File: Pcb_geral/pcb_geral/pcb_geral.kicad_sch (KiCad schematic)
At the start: 29 parts, among them U1 LM2594M-3.3, U2 LM2596S-5, U3 STM32F103C6Tx, U4 TJA1051T, Y2 8Mhz

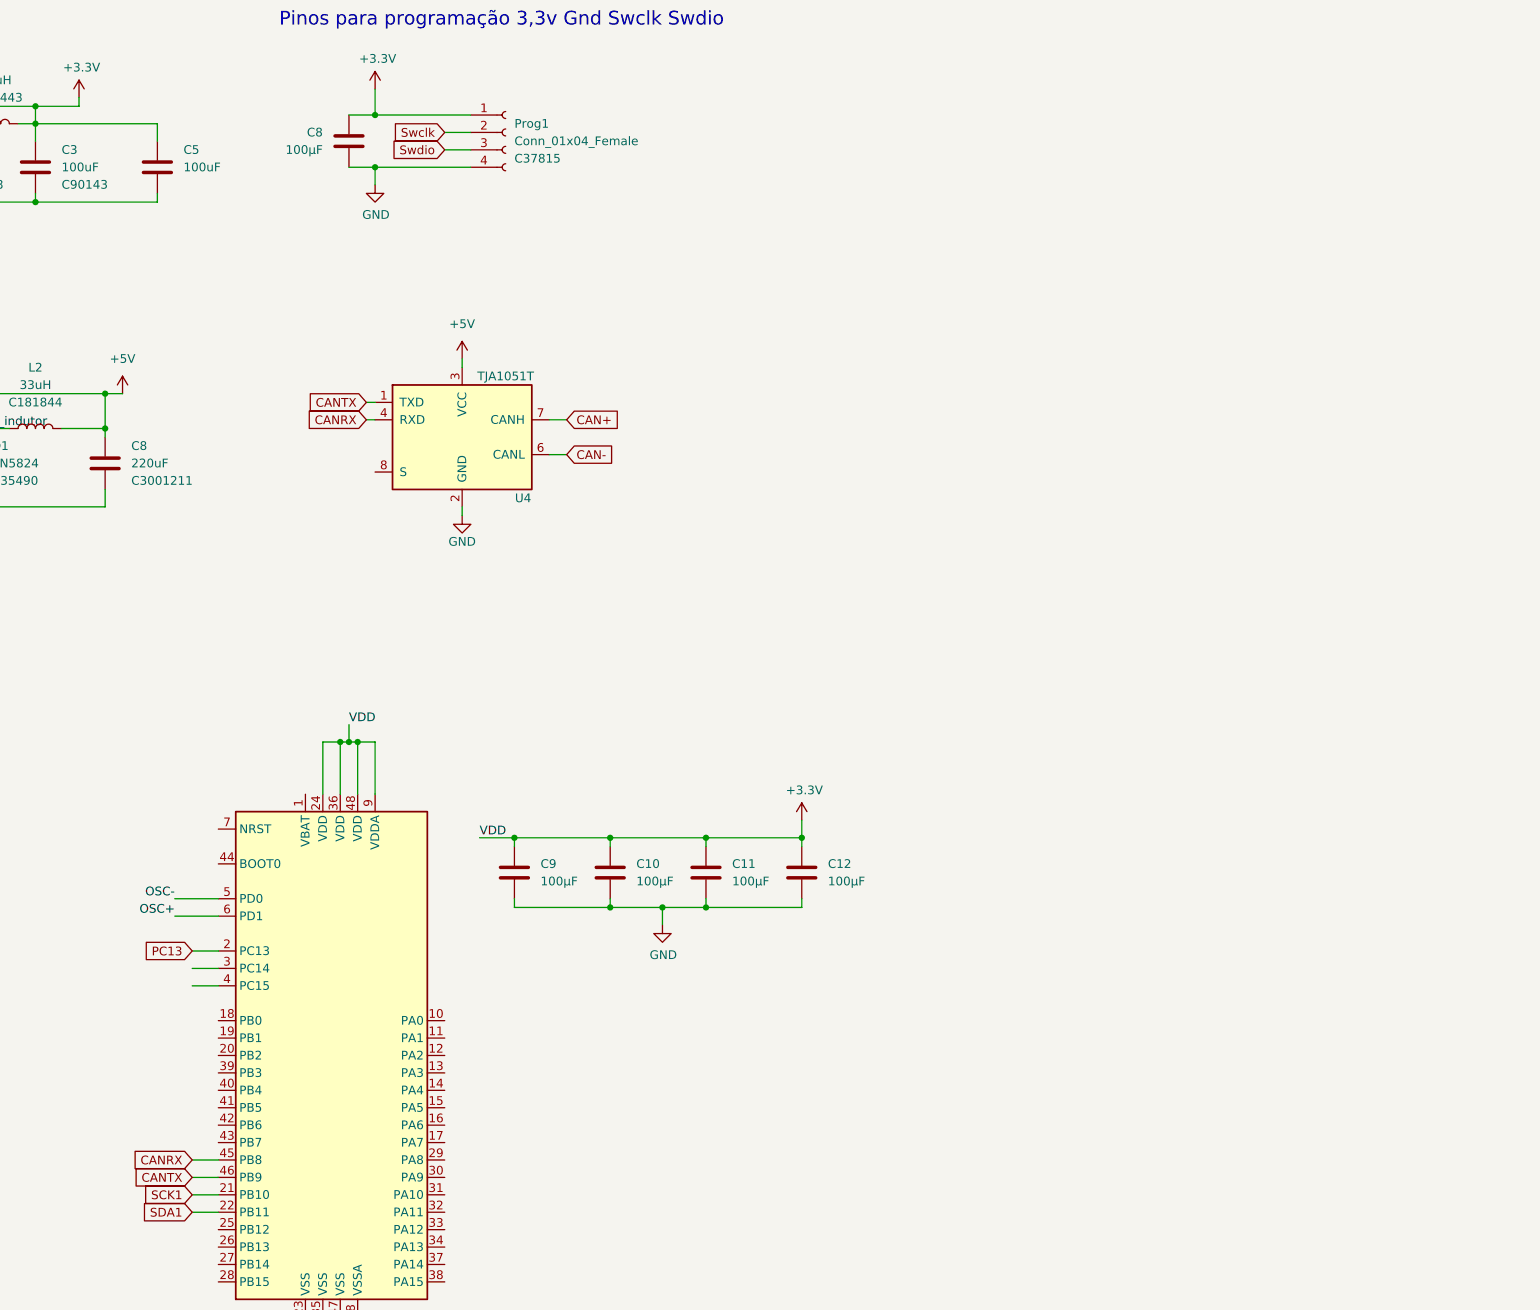
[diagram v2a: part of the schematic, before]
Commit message: placa geral, add can e footprints
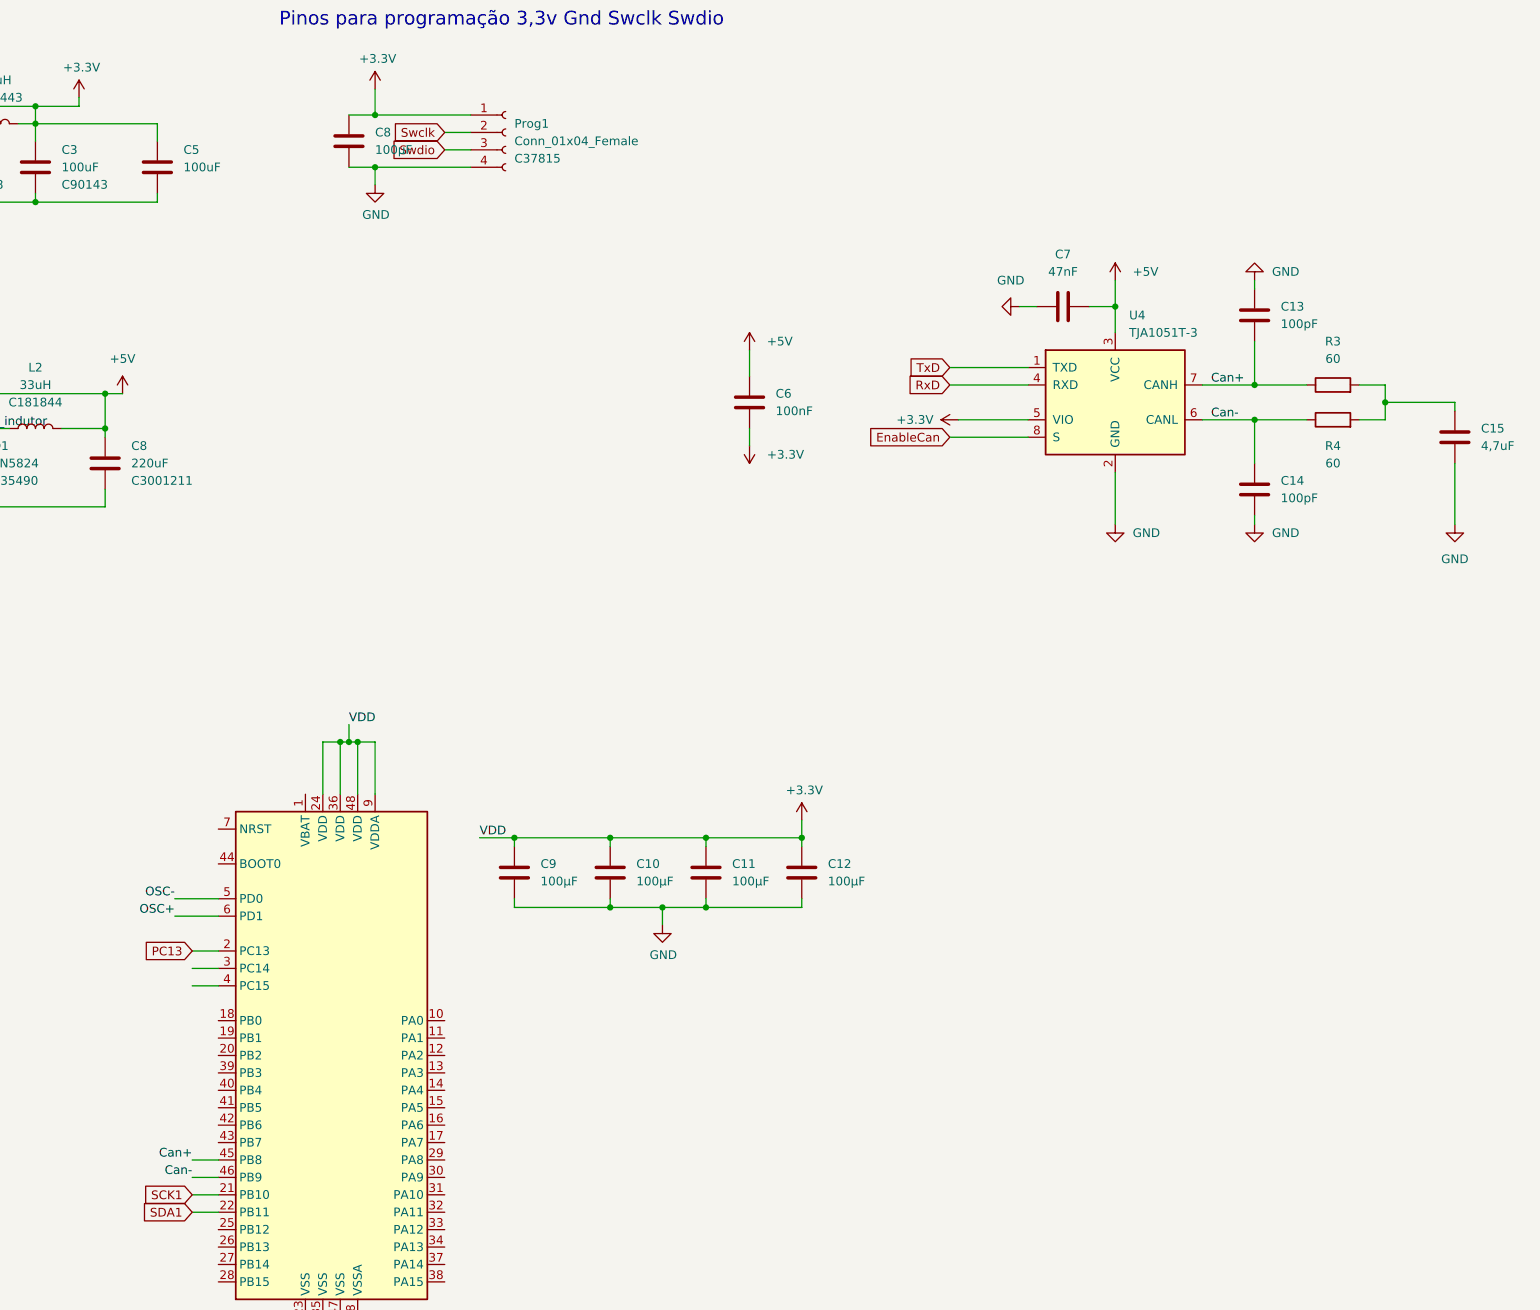
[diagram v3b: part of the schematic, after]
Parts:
- removed U4: TJA1051T, Package_SO:SOIC-8_3.9x4.9mm_P1.27mm, symbol Interface_CAN_LIN:TJA1051T
- added C13, C14: 100pF, Capacitor_SMD:C_0603_1608Metric_Pad1.08x0.95mm_HandSolder, symbol Device:C
- added C15: 4,7uF, Capacitor_SMD:C_0603_1608Metric_Pad1.08x0.95mm_HandSolder, symbol Device:C
- added C6: 100nF, Capacitor_SMD:C_0603_1608Metric_Pad1.08x0.95mm_HandSolder, symbol Device:C
- added C7: 47nF, Capacitor_SMD:C_0603_1608Metric_Pad1.08x0.95mm_HandSolder, symbol Device:C
- added R3, R4: 60, Resistor_SMD:R_0603_1608Metric_Pad0.98x0.95mm_HandSolder, symbol Device:R
- added U4: TJA1051T-3, Package_SO:SOIC-8_3.9x4.9mm_P1.27mm, symbol Interface_CAN_LIN:TJA1051T-3
- C8: footprint (none) -> Capacitor_SMD:C_0603_1608Metric_Pad1.08x0.95mm_HandSolder
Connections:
- net +3V3: now also C6.1, U4.5 (VIO)
- net +5V: now also C6.2, C7.1, U4.3 (VCC)
- net GND: now also C13.1, C14.1, C15.1, C7.2, U4.2 (GND)
- net CANRX renamed Can+
- net Can+: now also C13.2, R3.1, U4.7 (CANH)
- net CANTX renamed Can-
- net Can-: now also C14.2, R4.1, U4.6 (CANL)
- new net: C15.2, R3.2, R4.2
- new net EnableCan: U4.8 (S)
- new net RxD: U4.4 (RXD)
- new net TxD: U4.1 (TXD)

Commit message: atualizacoes na placa geral, posicionamento do can, adição dos pontos para conexão para sensores e dispositivos externos, sistemas de proteção contra corrente excessiva e reversão de tensão, silk mais detalhado entre outros
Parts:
- added F?: Fuse, symbol Device:Fuse
- added J1: Conn_01x04_Female, TerminalBlock_Phoenix:TerminalBlock_Phoenix_MKDS-1,5-4_1x04_P5.00mm_Horizontal, symbol Connector:Conn_01x04_Female
- added J2, J3: Conn_01x03_Female, Connector_PinHeader_2.54mm:PinHeader_1x03_P2.54mm_Vertical, symbol Connector:Conn_01x03_Female
- added J4: Conn_01x04_Female, symbol Connector:Conn_01x04_Female
- added J5, J6: Conn_01x04_Female, Connector_PinHeader_2.54mm:PinHeader_1x04_P2.54mm_Vertical, symbol Connector:Conn_01x04_Female
- added Q?: Q_NMOS_GDS, symbol Device:Q_NMOS_GDS
- D3, D4: footprint (none) -> LED_SMD:LED_0603_1608Metric_Pad1.05x0.95mm_HandSolder
- R1, R2: footprint (none) -> Resistor_SMD:R_0603_1608Metric
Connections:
- net +12V: now also J2.1 (Pin_1), Q?.2 (D)
- net +5V: now also J4.1 (Pin_1), J5.1 (Pin_1)
- net Can+: now also J1.3 (Pin_3); no longer U3.45 (PB8)
- net Can-: now also J1.2 (Pin_2); no longer U3.46 (PB9)
- net GND: now also J1.4 (Pin_4), J2.3 (Pin_3), J4.4 (Pin_4), J5.4 (Pin_4), Q?.1 (G)
- net PC13: now also R1.1; no longer R1.2
- net SCK1: now also J4.2 (Pin_2)
- net SDA1: now also J4.3 (Pin_3)
- net at D3.1 (K): now also R1.2; no longer R1.1
- new net: F?.1, J1.1 (Pin_1)
- new net: F?.2, Q?.3 (S)
- new net RX: J5.3 (Pin_3)
- new net TX: J5.2 (Pin_2)
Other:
- note added: "Fita de Led"
- note added: "GPS"
- note added: "I2C"
- note added: "Proteção contra corrente reversa e fusível"
- note added: "Qual protocolo para Fita de led? Exemplo Fita de Led STM32 5v ou 12V?"
- note added: "Qual é o protocolo para comunicar o GPS?"
- note added: "Sensor de Velocidade"
- note added: "Sensor de combustível"
- note added: "Sensor de temperatura"
- note added: "Vai ter uma placa para o sensor de combustível? ou vai ter sensor capacitivo"
- note added: "colocar opto acoplador"
- moved on the sheet: C10, C11, C12, C13, C14, C15, C6, C7, C9, D4, R1, R2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
